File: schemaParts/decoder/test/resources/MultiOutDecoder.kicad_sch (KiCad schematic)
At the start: 6 parts, among them U1 74LS156

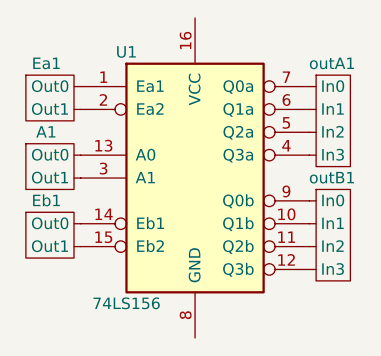
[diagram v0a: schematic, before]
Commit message: MultiOutDecoder - Optimiser, Complete Reverse/OpenCollector suppor, Unittest Fix. Decodes - simplify.
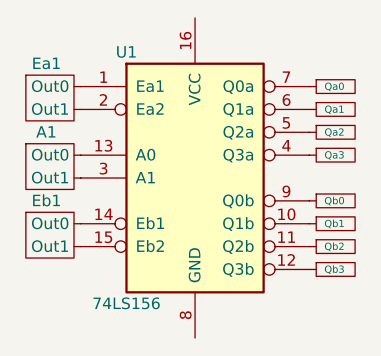
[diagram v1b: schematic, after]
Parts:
- removed outA1, outB1: InBus4x, symbol Tests:InBus4x
- added Qa0, Qa1, Qa2, Qa3, Qb0, Qb1, Qb2, Qb3: InPin, symbol Tests:InPin
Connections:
- net at U1.10 (Q1b): now also Qb1.1 (In)
- net at U1.11 (Q2b): now also Qb2.1 (In)
- net at U1.12 (Q3b): now also Qb3.1 (In)
- net at U1.4 (Q3a): now also Qa3.1 (In)
- net at U1.5 (Q2a): now also Qa2.1 (In)
- net at U1.6 (Q1a): now also Qa1.1 (In)
- net at U1.7 (Q0a): now also Qa0.1 (In)
- net at U1.9 (Q0b): now also Qb0.1 (In)
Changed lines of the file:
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@@
     )
   )
-  (symbol (lib_id "Tests:InBus4x") (at 195.58 76.2 0) (unit 1)
-    (in_bom yes) (on_board yes) (dnp no)
-    (property "Reference" "outA1" (at 198.12 69.85 0)
-      (effects (font (size 1.27 1.27)))
-    )
-    (property "Value" "InBus4x" (at 186.678 70.612 0)
-      (effects (font (size 1.27 1.27)) hide)
-    )
-    (property "Footprint" "" (at 196.33 81.28 0)
-      (effects (font (size 1.27 1.27)) hide)
-    )
-    (property "Datasheet" "" (at 196.33 81.28 0)
-      (effects (font (size 1.27 1.27)) hide)
-    )
-    (pin "1")
-    (pin "0")
-    (pin "3")
-    (pin "2")
-    (instances
-      (project "MultiOutDecoder"
-        (path "/dca00733-6e59-4b89-b3a6-bb50926963b6"
-          (reference "outA1") (unit 1)
+  (symbol (lib_id "Tests:InPin") (at 195.58 77.47 0) (unit 1)
+    (in_bom yes) (on_board yes) (dnp no)
+    (property "Reference" "Qa2" (at 198.374 77.47 0)
+      (effects (font (size 0.8 0.8)))
+    )
+    (property "Value" "InPin" (at 194.31 71.374 0)
+      (effects (font (size 1.27 1.27)) hide)
+    )
+    (property "Footprint" "" (at 195.58 77.47 0)
+      (effects (font (size 1.27 1.27)) hide)
+    )
+    (property "Datasheet" "" (at 195.58 77.47 0)
+      (effects (font (size 1.27 1.27)) hide)
+    )
+    (pin "1")
+    (instances
+      (project "MultiOutDecoder"
+        (path "/dca00733-6e59-4b89-b3a6-bb50926963b6"
+          (reference "Qa2") (unit 1)
+        )
+      )
+    )
+  )
+  (symbol (lib_id "Tests:InPin") (at 195.58 80.01 0) (unit 1)
+    (in_bom yes) (on_board yes) (dnp no)
+    (property "Reference" "Qa3" (at 198.374 80.01 0)
+      (effects (font (size 0.8 0.8)))
+    )
+    (property "Value" "InPin" (at 194.31 73.914 0)
+      (effects (font (size 1.27 1.27)) hide)
+    )
+    (property "Footprint" "" (at 195.58 80.01 0)
+      (effects (font (size 1.27 1.27)) hide)
+    )
+    (property "Datasheet" "" (at 195.58 80.01 0)
+      (effects (font (size 1.27 1.27)) hide)
+    )
+    (pin "1")
+    (instances
+      (project "MultiOutDecoder"
+        (path "/dca00733-6e59-4b89-b3a6-bb50926963b6"
+          (reference "Qa3") (unit 1)
+        )
+      )
+    )
+  )
+  (symbol (lib_id "Tests:InPin") (at 195.58 85.09 0) (unit 1)
+    (in_bom yes) (on_board yes) (dnp no)
+    (property "Reference" "Qb0" (at 198.374 85.09 0)
+      (effects (font (size 0.8 0.8)))
+    )
+    (property "Value" "InPin" (at 194.31 78.994 0)
+      (effects (font (size 1.27 1.27)) hide)
+    )
+    (property "Footprint" "" (at 195.58 85.09 0)
+      (effects (font (size 1.27 1.27)) hide)
+    )
+    (property "Datasheet" "" (at 195.58 85.09 0)
+      (effects (font (size 1.27 1.27)) hide)
+    )
+    (pin "1")
+    (instances
+      (project "MultiOutDecoder"
+        (path "/dca00733-6e59-4b89-b3a6-bb50926963b6"
+          (reference "Qb0") (unit 1)
         )
       )
@@
     )
   )
-  (symbol (lib_id "Tests:InBus4x") (at 195.58 88.9 0) (unit 1)
-    (in_bom yes) (on_board yes) (dnp no)
-    (property "Reference" "outB1" (at 198.12 82.55 0)
-      (effects (font (size 1.27 1.27)))
-    )
-    (property "Value" "InBus4x" (at 186.678 83.312 0)
-      (effects (font (size 1.27 1.27)) hide)
-    )
-    (property "Footprint" "" (at 196.33 93.98 0)
-      (effects (font (size 1.27 1.27)) hide)
-    )
-    (property "Datasheet" "" (at 196.33 93.98 0)
-      (effects (font (size 1.27 1.27)) hide)
-    )
-    (pin "1")
-    (pin "0")
-    (pin "3")
-    (pin "2")
-    (instances
-      (project "MultiOutDecoder"
-        (path "/dca00733-6e59-4b89-b3a6-bb50926963b6"
-          (reference "outB1") (unit 1)
-        )
-      )
+  (symbol (lib_id "Tests:InPin") (at 195.58 92.71 0) (unit 1)
+    (in_bom yes) (on_board yes) (dnp no)
+    (property "Reference" "Qb3" (at 198.374 92.71 0)
+      (effects (font (size 0.8 0.8)))
+    )
+    (property "Value" "InPin" (at 194.31 86.614 0)
+      (effects (font (size 1.27 1.27)) hide)
+    )
+    (property "Footprint" "" (at 195.58 92.71 0)
+      (effects (font (size 1.27 1.27)) hide)
+    )
+    (property "Datasheet" "" (at 195.58 92.71 0)
+      (effects (font (size 1.27 1.27)) hide)
+    )
+    (pin "1")
+    (instances
+      (project "MultiOutDecoder"
+        (path "/dca00733-6e59-4b89-b3a6-bb50926963b6"
+          (reference "Qb3") (unit 1)
+        )
+      )
+    )
+  )
+  (symbol (lib_id "Tests:InPin") (at 195.58 74.93 0) (unit 1)
+    (in_bom yes) (on_board yes) (dnp no)
+    (property "Reference" "Qa1" (at 198.374 74.93 0)
+      (effects (font (size 0.8 0.8)))
+    )
+    (property "Value" "InPin" (at 194.31 68.834 0)
+      (effects (font (size 1.27 1.27)) hide)
+    )
+    (property "Footprint" "" (at 195.58 74.93 0)
+      (effects (font (size 1.27 1.27)) hide)
+    )
+    (property "Datasheet" "" (at 195.58 74.93 0)
+      (effects (font (size 1.27 1.27)) hide)
+    )
+    (pin "1")
+    (instances
+      (project "MultiOutDecoder"
+        (path "/dca00733-6e59-4b89-b3a6-bb50926963b6"
+          (reference "Qa1") (unit 1)
+        )
+      )
+    )
+  )
+  (symbol (lib_id "Tests:InPin") (at 195.58 87.63 0) (unit 1)
+    (in_bom yes) (on_board yes) (dnp no)
+    (property "Reference" "Qb1" (at 198.374 87.63 0)
+      (effects (font (size 0.8 0.8)))
+    )
+    (property "Value" "InPin" (at 194.31 81.534 0)
+      (effects (font (size 1.27 1.27)) hide)
+    )
+    (property "Footprint" "" (at 195.58 87.63 0)
+      (effects (font (size 1.27 1.27)) hide)
+    )
+    (property "Datasheet" "" (at 195.58 87.63 0)
+      (effects (font (size 1.27 1.27)) hide)
+    )
+    (pin "1")
+    (instances
+      (project "MultiOutDecoder"
+        (path "/dca00733-6e59-4b89-b3a6-bb50926963b6"
+          (reference "Qb1") (unit 1)
+        )
+      )
+    )
+  )
+  (symbol (lib_id "Tests:InPin") (at 195.58 72.39 0) (unit 1)
+    (in_bom yes) (on_board yes) (dnp no)
+    (property "Reference" "Qa0" (at 198.374 72.39 0)
+      (effects (font (size 0.8 0.8)))
+    )
+    (property "Value" "InPin" (at 194.31 66.294 0)
+      (effects (font (size 1.27 1.27)) hide)
+    )
+    (property "Footprint" "" (at 195.58 72.39 0)
+      (effects (font (size 1.27 1.27)) hide)
+    )
+    (property "Datasheet" "" (at 195.58 72.39 0)
+      (effects (font (size 1.27 1.27)) hide)
+    )
+    (pin "1")
+    (instances
+      (project "MultiOutDecoder"
+        (path "/dca00733-6e59-4b89-b3a6-bb50926963b6"
+          (reference "Qa0") (unit 1)
+        )
+      )
+    )
+  )
+  (symbol (lib_id "Tests:InPin") (at 195.58 90.17 0) (unit 1)
+    (in_bom yes) (on_board yes) (dnp no)
+    (property "Reference" "Qb2" (at 198.374 90.17 0)
+      (effects (font (size 0.8 0.8)))
+    )
+    (property "Value" "InPin" (at 194.31 84.074 0)
+      (effects (font (size 1.27 1.27)) hide)
+    )
+    (property "Footprint" "" (at 195.58 90.17 0)
+      (effects (font (size 1.27 1.27)) hide)
+    )
+    (property "Datasheet" "" (at 195.58 90.17 0)
+      (effects (font (size 1.27 1.27)) hide)
+    )
+    (pin "1")
+    (instances
+      (project "MultiOutDecoder"
+        (path "/dca00733-6e59-4b89-b3a6-bb50926963b6"
+          (reference "Qb2") (unit 1)
+        )
+      )
